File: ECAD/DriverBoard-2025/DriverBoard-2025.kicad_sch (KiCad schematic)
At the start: 18 parts, among them J1 XT30, J2 Conn_01x04, J3 Conn_01x04, J4 Conn_01x04, U1 TMC2209_SILENTSTEPSTICK, U2 TMC2209_SILENTSTEPSTICK, U3 TMC2209_SILENTSTEPSTICK

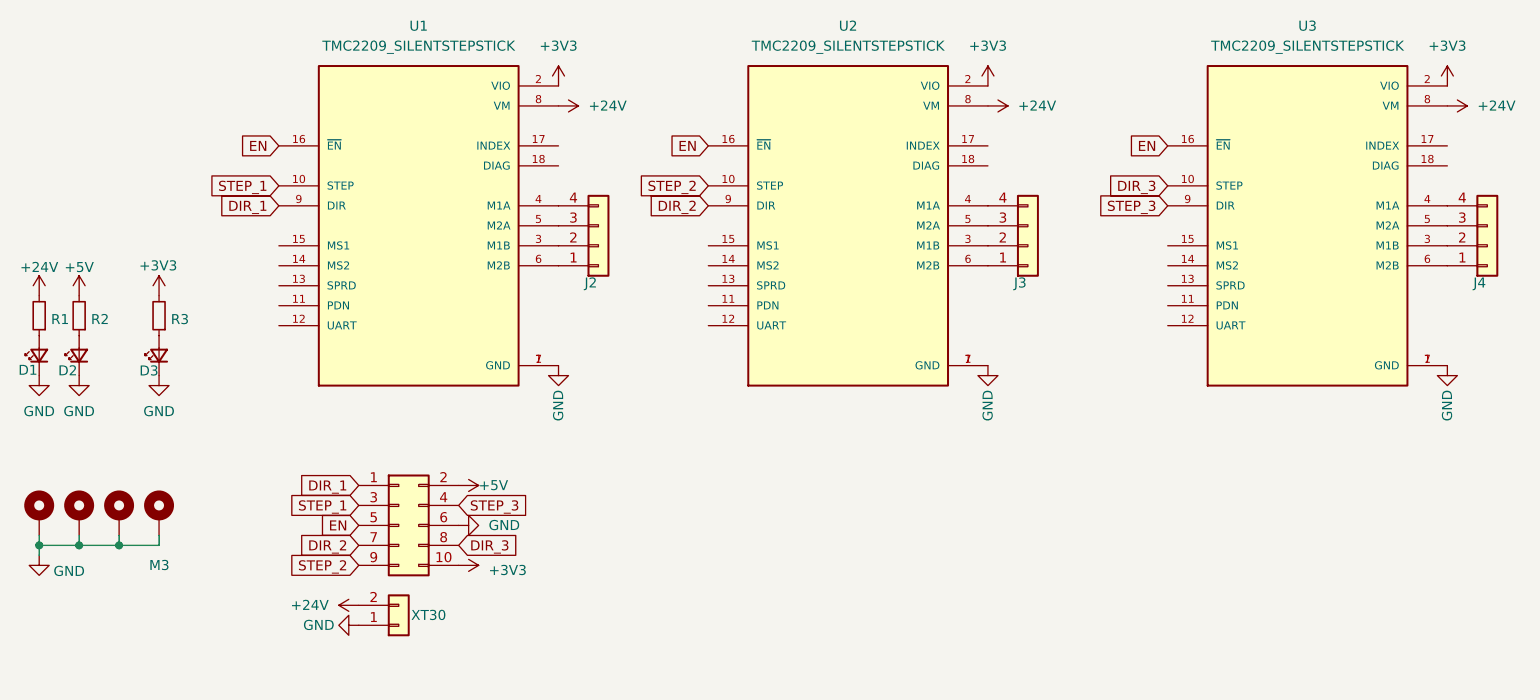
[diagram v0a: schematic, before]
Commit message: Ad microstepping and capacitors
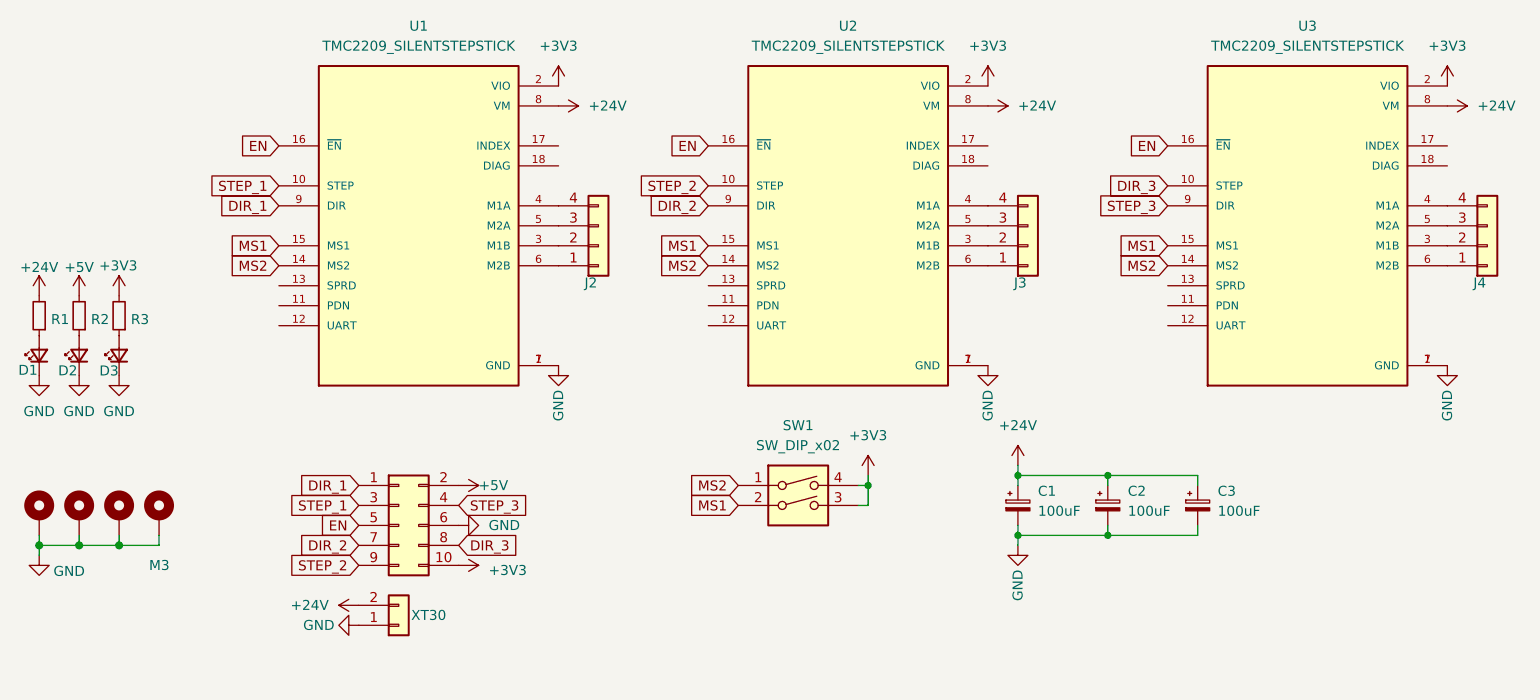
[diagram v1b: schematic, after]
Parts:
- added C1, C2, C3: 100uF, Capacitor_THT:CP_Radial_D8.0mm_P3.50mm, symbol Device:C_Polarized_Small
- added SW1: SW_DIP_x02, Button_Switch_THT:SW_DIP_SPSTx02_Slide_9.78x7.26mm_W7.62mm_P2.54mm, symbol Switch:SW_DIP_x02
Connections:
- net +24V: now also C1.1, C2.1, C3.1
- net +3V3: now also SW1.3, SW1.4
- net GND: now also C1.2, C2.2, C3.2
- net MS2: now reaches U2.14 (MS2)
- net MS2: now also U1.14 (MS2), U3.14 (MS2), SW1.1
- net MS1: now reaches U2.15 (MS1)
- net MS1: now also U1.15 (MS1), U3.15 (MS1), SW1.2
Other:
- moved on the sheet: D3, R3

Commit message: Premier routage
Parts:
- added J5: Fan, Connector_Molex:Molex_KK-254_AE-6410-02A_1x02_P2.54mm_Vertical, symbol Connector_Generic:Conn_01x02
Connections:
- net +5V: now also J5.1 (Pin_1)
- net GND: now also J5.2 (Pin_2)
- net at J2.2 (Pin_2): now also U1.5 (M2A); no longer U1.3 (M1B)
- net at J2.3 (Pin_3): now also U1.4 (M1A); no longer U1.5 (M2A)
- net at J2.4 (Pin_4): now also U1.3 (M1B); no longer U1.4 (M1A)
- net at U2.3 (M1B): now also J3.4 (Pin_4); no longer J3.2 (Pin_2)
- net at U2.4 (M1A): now also J3.3 (Pin_3); no longer J3.4 (Pin_4)
- net at U2.5 (M2A): now also J3.2 (Pin_2); no longer J3.3 (Pin_3)
- net at U3.3 (M1B): now also J4.4 (Pin_4); no longer J4.2 (Pin_2)
- net at J4.3 (Pin_3): now also U3.4 (M1A); no longer U3.5 (M2A)
- new net: J4.2 (Pin_2), U3.5 (M2A)
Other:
- moved on the sheet: J2, J3, J4

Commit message: PCB routing completed
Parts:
- SW1: footprint Button_Switch_THT:SW_DIP_SPSTx02_Slide_9.78x7.26mm_W7.62mm_P2.54mm -> Connector_PinHeader_2.54mm:PinHeader_2x02_P2.54mm_Vertical
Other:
- moved on the sheet: J4
